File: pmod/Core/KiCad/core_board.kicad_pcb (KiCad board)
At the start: 4 copper layers, 100 x 66 mm, 90 parts, among them J1 Conn_01x04_Pin, J10 Conn_01x04, J11 USB_B_Micro, J12 USB_C_Receptacle_USB2.0, J13 Conn_01x03, J14 Conn_01x04_Pin, J2 PMOD0_FULL, J3 Conn_01x06, J4 Conn_01x06, J6 Conn_01x10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

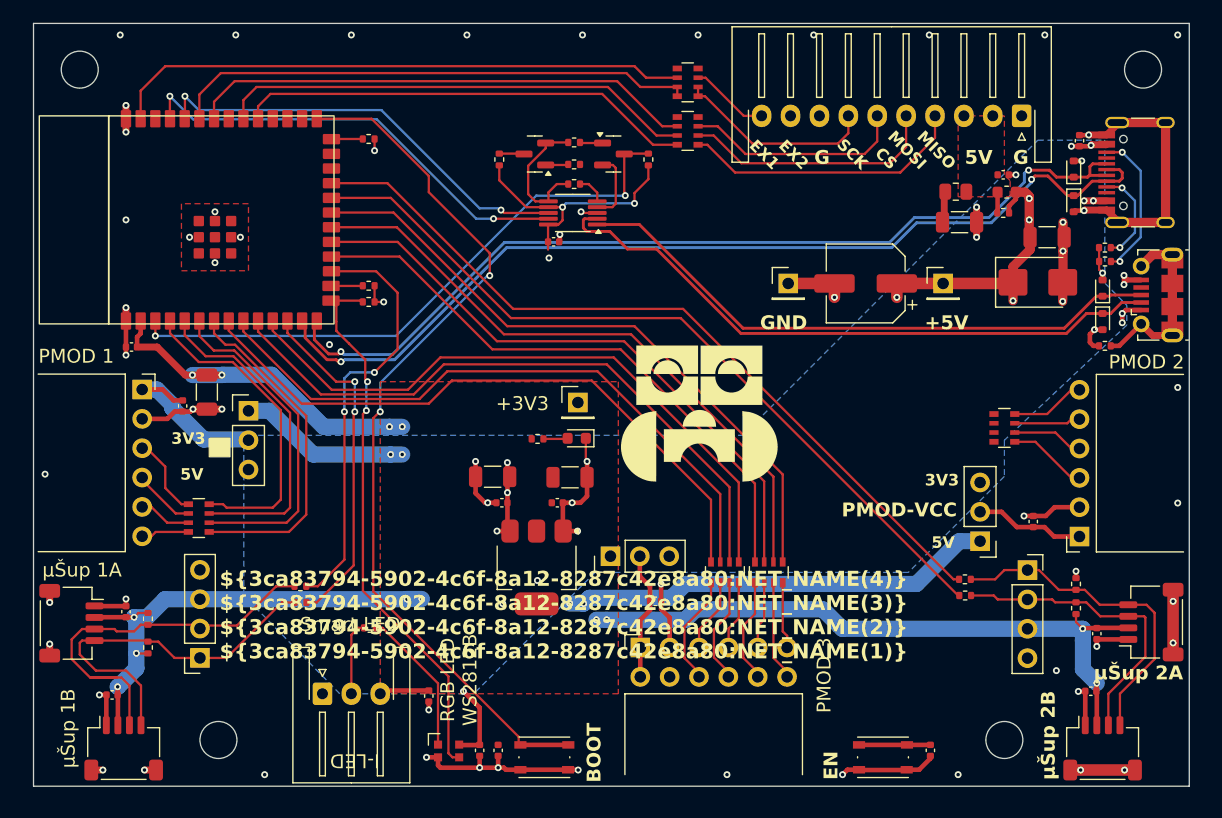
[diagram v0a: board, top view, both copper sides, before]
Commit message: core_board/Saturn: add review hw version
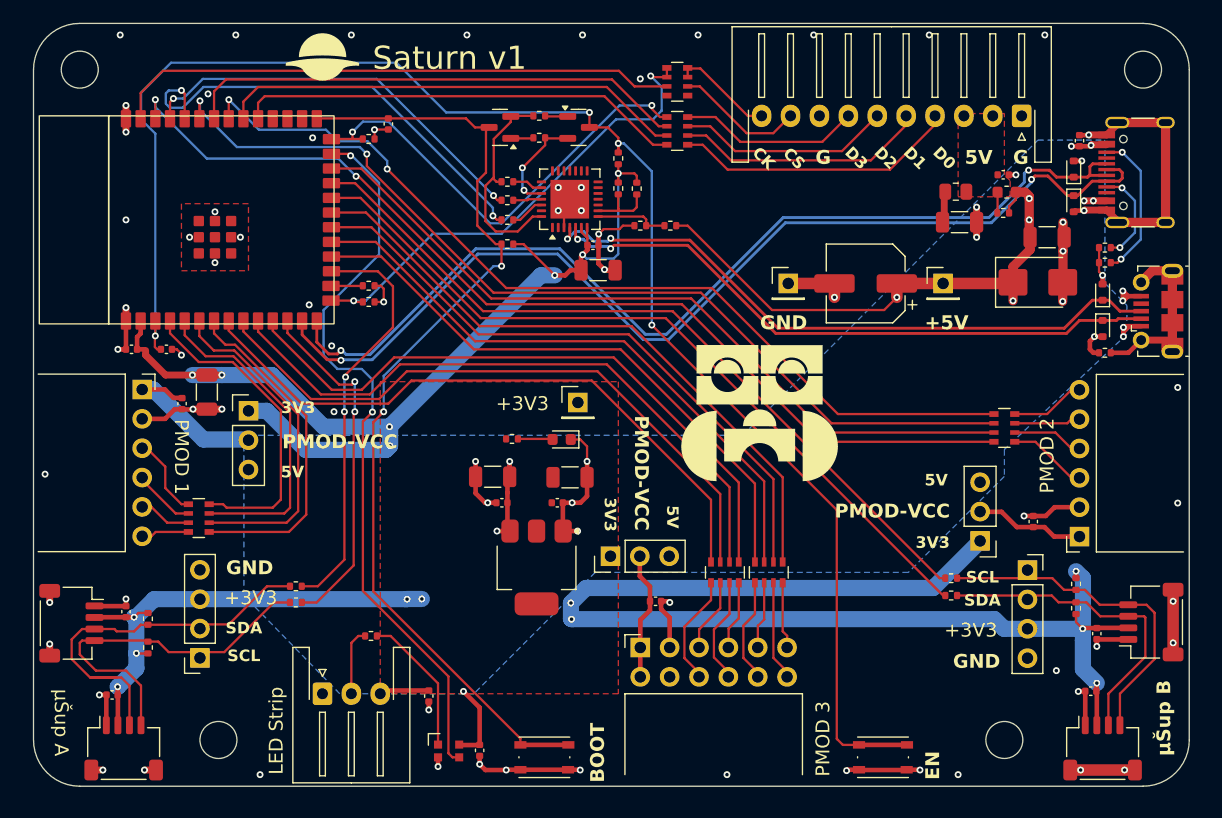
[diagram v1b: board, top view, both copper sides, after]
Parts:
- removed U6: CH340X, Package_SO:MSOP-10_3x3mm_P0.5mm
- added C24: 10u, Capacitor_SMD:C_1206_3216Metric, F.Cu at (93.8, 77.3)
- added R10: 2k, Resistor_SMD:R_0402_1005Metric, F.Cu at (95.6, 70.3)
- added R11: 10k, Resistor_SMD:R_0402_1005Metric, F.Cu at (97.5, 73.5)
- added R12: 5k1, Resistor_SMD:R_0402_1005Metric, F.Cu at (100.1, 73.5)
- added R13: 2k, Resistor_SMD:R_0402_1005Metric, F.Cu at (97.2, 70.3)
- added R17: 100R, Resistor_SMD:R_0402_1005Metric, F.Cu at (86.0, 73.0)
- added R18: 100R, Resistor_SMD:R_0402_1005Metric, F.Cu at (86.0, 71.3)
- added U3: CP2102N-Axx-xQFN28, Package_DFN_QFN:QFN-28-1EP_5x5mm_P0.5mm_EP3.35x3.35mm, F.Cu at (91.4, 71.2)
- moved C17 74.7 mm to (56.5, 84.2), turned to 0 degrees
- moved C18 55.0 mm to (75.7, 64.7)
- moved R1 7.36 mm to (86.0, 75.1), turned to 0 degrees
- moved R34 5.78 mm to (86.0, 69.7)
- moved R36 3.80 mm to (88.8, 65.9)
- moved R35 3.80 mm to (88.8, 64.0)
- moved Q3 3.80 mm to (92.2, 65.0)
- moved Q4 3.80 mm to (85.4, 65.0)
- moved C14 3.41 mm to (93.4, 75.2)
- moved R2 2.61 mm to (95.6, 67.7)
- moved R5 2.21 mm to (86.4, 92.0)
- moved J11 1.40 mm to (142.3, 80.9)
- moved D2 1.30 mm to (90.7, 92.0)
- moved R6 1.21 mm to (124.4, 105.5)
- moved R4 1.19 mm to (124.4, 104.0)
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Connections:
- net /DISPLAY_MISO renamed /DISPLAY_IO0
- net /DISPLAY_MOSI renamed /DISPLAY_IO1
- net /I2C1_SCL renamed /I2CA_SCL
- net /I2C1_SDA renamed /I2CA_SDA
- net /I2C2_SCL renamed /I2CB_SCL
- net /I2C2_SDA renamed /I2CB_SDA
- J6 pad 9: unconnected-(J6-Pin_9-Pad9) -> Net-(J6-Pin_9)
- R14 pad 2: /SMART_LEDS -> /DISPLAY_CLK
- R15 pad 2: Net-(U1-IO45-PD) -> /DISPLAY_IO3
- RN5 pad 4: (no net) -> Net-(J6-Pin_7)
- RN5 pad 5: (no net) -> /DISPLAY_IO3
- RN5 pad 6: /DISPLAY_CS -> /DISPLAY_IO2
- RN6 pad 1: Net-(J6-Pin_7) -> unconnected-(RN6A-R1.1-Pad1)
- RN6 pad 2: Net-(J6-Pin_7) -> Net-(J6-Pin_9)
- RN6 pad 4: (no net) -> Net-(J6-Pin_10)
- RN6 pad 5: (no net) -> /DISPLAY_CLK
- RN6 pad 6: /DISPLAY_EX1 -> /DISPLAY_CLK
- RN6 pad 7: /DISPLAY_CLK -> /DISPLAY_CS
- RN6 pad 8: /DISPLAY_CLK -> unconnected-(RN6A-R1.2-Pad8)
- U1 pad 15: /SMART_LEDS -> /DISPLAY_CLK
- U1 pad 25: /PMOD2_IO2 -> /SMART_LEDS
- U1 pad 26: Net-(U1-IO45-PD) -> /DISPLAY_IO3
- U1 pad 34: /DISPLAY_CS -> /DISPLAY_IO2
- U1 pad 35: /DISPLAY_CLK -> /PMOD2_IO2
- U1 pad 39: /DISPLAY_EX1 -> /DISPLAY_CS
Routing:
- net /PMOD2_IO4: track 0.00 -> 86.8 mm, vias 0 -> 2
- net /PMOD2_IO2: track 0.00 -> 82.9 mm, vias 0 -> 2
- net /PMOD2_IO1: track 0.00 -> 79.5 mm, vias 0 -> 2
- net /EN: track 59.0 -> 138.2 mm, vias 2 -> 4
- net /PMOD2_IO3: track 0.00 -> 66.8 mm
- net /DISPLAY_EX1: track 50.1 -> 0.00 mm
- net /DISPLAY_IO2: track 0.00 -> 43.7 mm
- net /DISPLAY_IO3: track 0.00 -> 39.6 mm, vias 0 -> 2
- net +3V3: track 205.5 -> 236.9 mm, vias 23 -> 17
- net +5V: track 50.4 -> 73.9 mm, vias 14 -> 13
- net /SMART_LEDS: track 47.6 -> 64.0 mm
- net Net-(J6-Pin_9): track 0.00 -> 11.2 mm
- net Net-(Q4-E): track 11.8 -> 18.6 mm
- net Net-(U3-VBUS): track 0.00 -> 6.38 mm
- net /USBMAIN_D+: track 80.9 -> 86.9 mm
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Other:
- outline, holes or cut-outs redrawn
- board text added: "+3V3"
- board text added: "CK"
- board text added: "D0"
- board text added: "D1"
- board text added: "D2"
- board text added: "D3"
- board text added: "GND"
- board text added: "LED Strip"
- board text added: "SCL"
- board text added: "SDA"
- board text added: "Saturn v1"
- board text added: "µŠup A"
- board text added: "µŠup B"
- board text removed: "${3ca83794-5902-4c6f-8a12-8287c42e8a80:NET_NAME(4)} ${3ca83794-5902-4c6f-8a12-8287c42e8a80:NET_NAME(3)} ${3ca83794-5902-4c6f-8a12-8287c42e8a80:NET_NAME(2)} ${3ca83794-5902-4c6f-8a12-8287c42e8a80:NET_NAME(1)}"
- board text removed: "EX1"
- board text removed: "EX2"
- board text removed: "MISO"
- board text removed: "MOSI"
- board text removed: "RGB LED WS2812B"
- board text removed: "SCK"
- board text removed: "Smart LED"
- board text removed: "µŠup 1A"
- board text removed: "µŠup 1B"
- board text removed: "µŠup 2A"
- board text removed: "µŠup 2B"

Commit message: core_board/Saturn: update review hw 2nd version
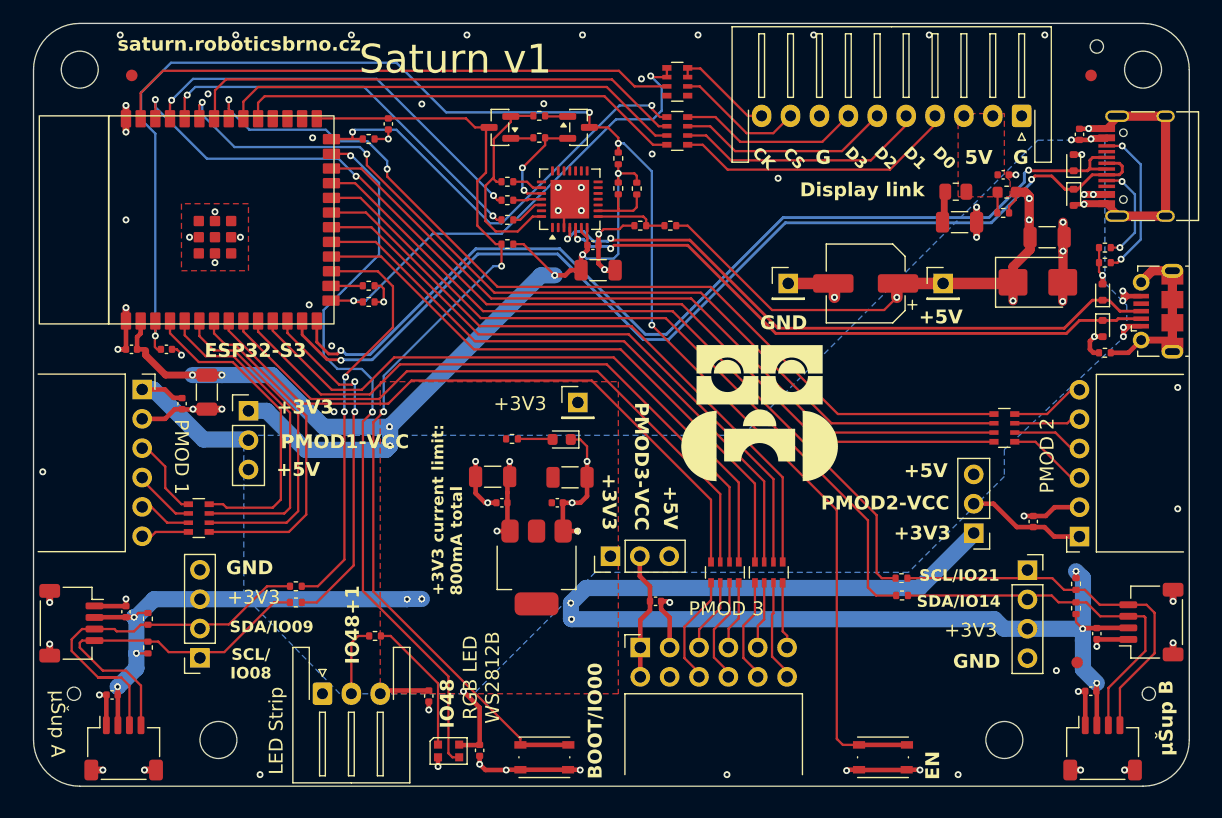
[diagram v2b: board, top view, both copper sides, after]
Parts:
- added FID1: Fiducial, Fiducial:Fiducial_1mm_Mask2mm, F.Cu at (53.5, 60.5)
- added FID2: Fiducial, Fiducial:Fiducial_1mm_Mask2mm, F.Cu at (136.5, 60.5)
- added FID3: Fiducial, Fiducial:Fiducial_1mm_Mask2mm, F.Cu at (135.3, 111.3)
- added H5: MountingHole, MountingHole:ToolingHole_1.152mm, F.Cu at (137.0, 58.0)
- added H6: MountingHole, MountingHole:ToolingHole_1.152mm, F.Cu at (48.5, 114.0)
- added H7: MountingHole, MountingHole:ToolingHole_1.152mm, F.Cu at (141.5, 114.0)
- C2: value EEEFK1H470XP -> RVT1V470M0605; footprint Capacitor_SMD:CP_Elec_6.3x7.7 -> Capacitor_SMD:CP_Elec_6.3x5.4
- moved R4 4.30 mm to (120.1, 104.0)
- moved R6 4.25 mm to (120.2, 105.5)
- moved JP3 0.87 mm to (126.3, 100.1)
- moved C19 0.55 mm to (135.5, 65.6)
- moved J12 0.55 mm to (141.9, 68.3)
- moved D6 0.55 mm to (135.0, 71.0)
- moved D7 0.55 mm to (135.0, 68.0)
- moved R33 0.35 mm to (74.5, 109.0)
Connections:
- RN6 pad 1: unconnected-(RN6A-R1.1-Pad1) -> (no net)
- RN6 pad 8: unconnected-(RN6A-R1.2-Pad8) -> (no net)
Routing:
- net GND: track 159.0 -> 147.7 mm, vias 82 -> 86
- net /ESP_RX_CP_TX: track 40.0 -> 34.4 mm
- net Net-(J1-Pin_1): track 29.9 -> 34.2 mm
- net Net-(J1-Pin_2): track 28.0 -> 32.3 mm
- net /I2CB_SCL: track 67.3 -> 65.9 mm
- net Net-(J14-Pin_2): track 34.6 -> 33.6 mm
- net /PMOD2_IO1: track 79.5 -> 80.4 mm
- net /I2CB_SDA: track 67.4 -> 66.5 mm
- net Net-(J4-Pin_6): track 9.49 -> 10.3 mm
- net /DISPLAY_IO3: track 39.6 -> 39.1 mm
- net /CC2: track 13.0 -> 13.5 mm
- net /CC1: track 8.35 -> 8.90 mm
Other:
- board text added: "+3V3 current limit: 800mA total"
- board text added: "+5V"
- board text added: "BOOT/IO00"
- board text added: "Display link"
- board text added: "ESP32-S3"
- board text added: "IO01"
- board text added: "IO03-PD"
- board text added: "IO04 IO05 IO06 IO07"
- board text added: "IO15 IO17 IO10 IO12"
- board text added: "IO16 IO18 IO11 IO13"
- board text added: "IO38"
- board text added: "IO39"
- board text added: "IO40 IO42 IO47 IO02"
- board text added: "IO41"
- board text added: "IO45-PD"
- board text added: "IO48"
- board text added: "IO48+1"
- board text added: "PMOD1-VCC"
- board text added: "PMOD2-VCC"
- board text added: "PMOD3-VCC"
- board text added: "Power from single source only"
- board text added: "RGB LED WS2812B"
- board text added: "SCL/ IO08"
- board text added: "SCL/IO21"
- board text added: "SDA/IO09"
- board text added: "SDA/IO14"
- board text added: "saturn.roboticsbrno.cz"
- board text removed: "3V3"
- board text removed: "BOOT"
- board text removed: "PMOD-VCC"
- board text removed: "SCL"
- board text removed: "SDA"

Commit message: core_board/Saturn: update review hw 2nd version
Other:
- board text added: "VCC"
